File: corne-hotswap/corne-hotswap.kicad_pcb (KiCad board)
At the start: 2 copper layers, 133.8 x 91.7 mm, 49 parts, among them J1 Battery Connector, J2 nice!view, J3 USB_C_Receptacle_PowerOnly_6P, J4 Battery Wire, SW1 SW_Push, SW10 SW_Push, SW11 SW_Push, SW12 SW_Push, SW13 SW_Push, SW14 SW_Push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

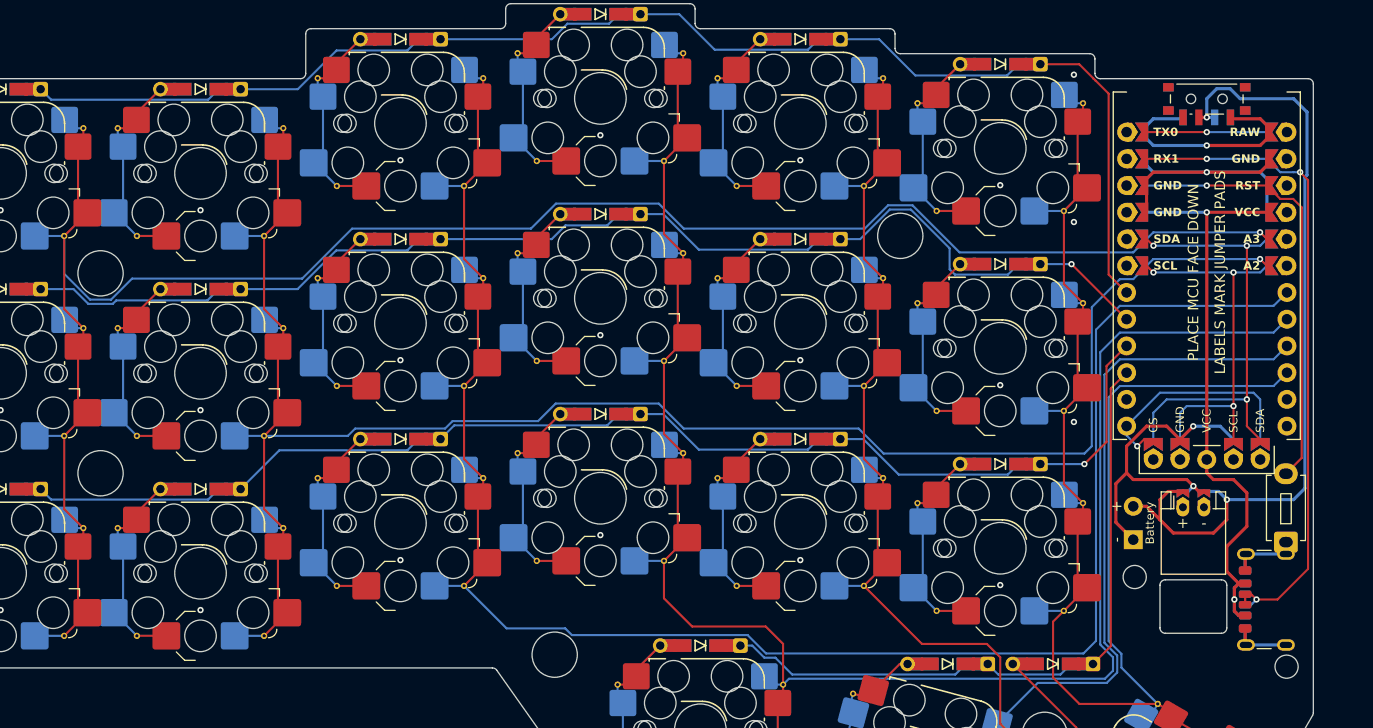
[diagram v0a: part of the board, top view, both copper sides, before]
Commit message: new design (using module)
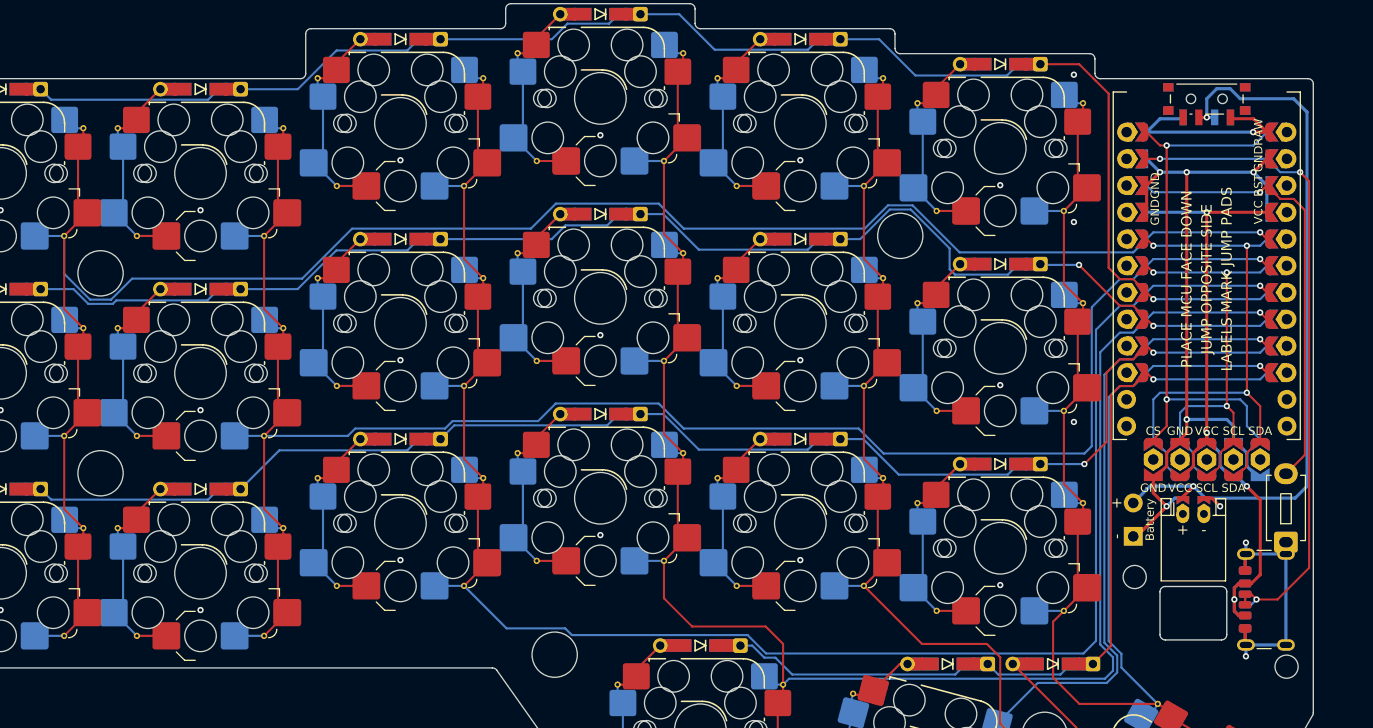
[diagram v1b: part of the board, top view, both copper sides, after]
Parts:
- moved J1 0.63 mm to (162.4, 82.4)
- moved J4 0.32 mm to (157.6, 84.5)
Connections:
- U1 pad 1: unconnected-(U1-D3-TX-Pad1)_1 -> CS
- U1 pad 12: CS -> unconnected-(U1-B5-Pad12)
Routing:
- net CS: track 22.2 -> 52.5 mm, vias 1 -> 2
- net GND: track 78.5 -> 99.6 mm, vias 24 -> 29
- net row1: track 106.2 -> 120.0 mm, vias 1 -> 2
- net row3: track 60.7 -> 74.2 mm, vias 0 -> 1
- net row0: track 120.2 -> 133.7 mm, vias 0 -> 1
- net row2: track 109.1 -> 122.5 mm, vias 1 -> 2
- net unconnected-(U1-D3-TX-Pad1)_1: track 11.4 -> 0.00 mm, vias 1 -> 0
- net SDA: track 42.9 -> 53.6 mm
- net SCL: track 35.7 -> 45.1 mm
- net battery: track 77.1 -> 69.4 mm
- net VCC: track 59.9 -> 64.9 mm, vias 2 -> 4
- net RAW: track 22.1 -> 19.5 mm
- net col5: track 85.8 -> 84.4 mm, vias 0 -> 1
- net col3: track 121.3 -> 119.9 mm, vias 0 -> 1
- net col2: track 131.4 -> 130.0 mm, vias 0 -> 1
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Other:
- outline, holes or cut-outs redrawn

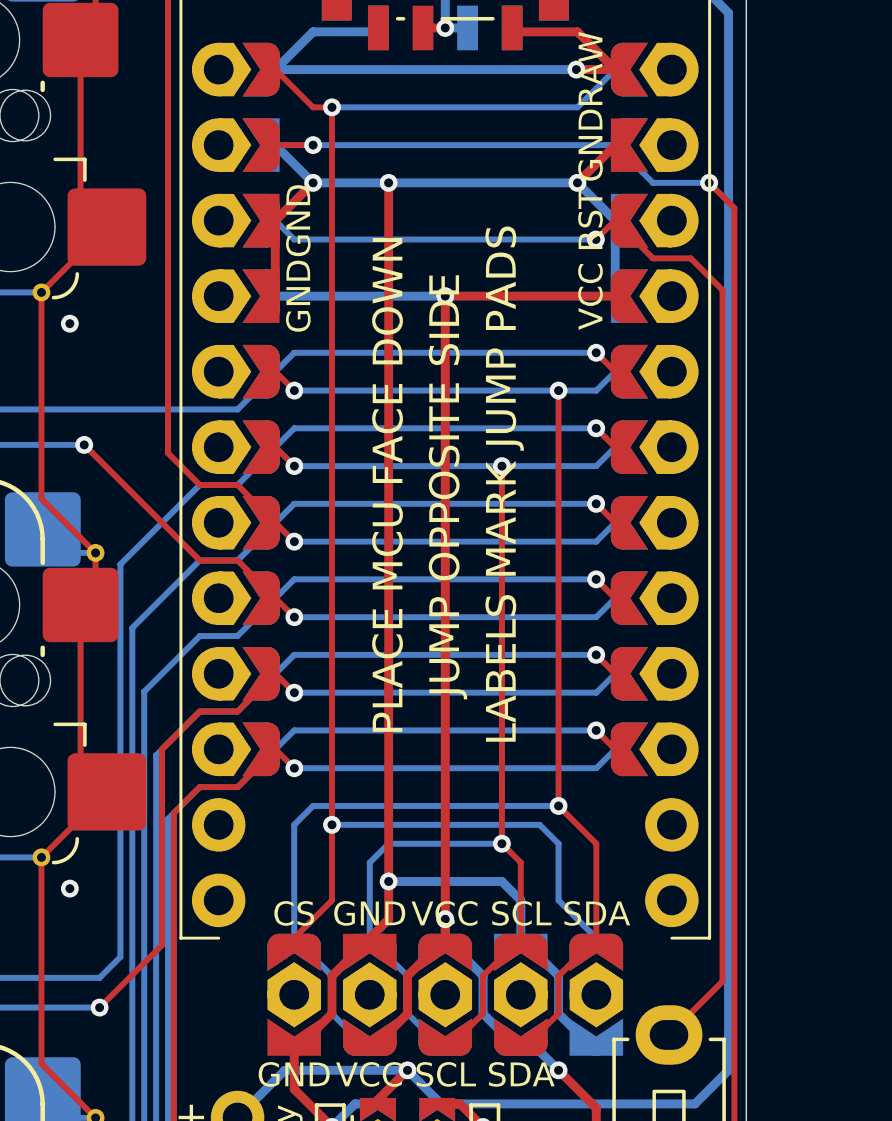
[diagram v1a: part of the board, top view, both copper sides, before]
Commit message: wiring update
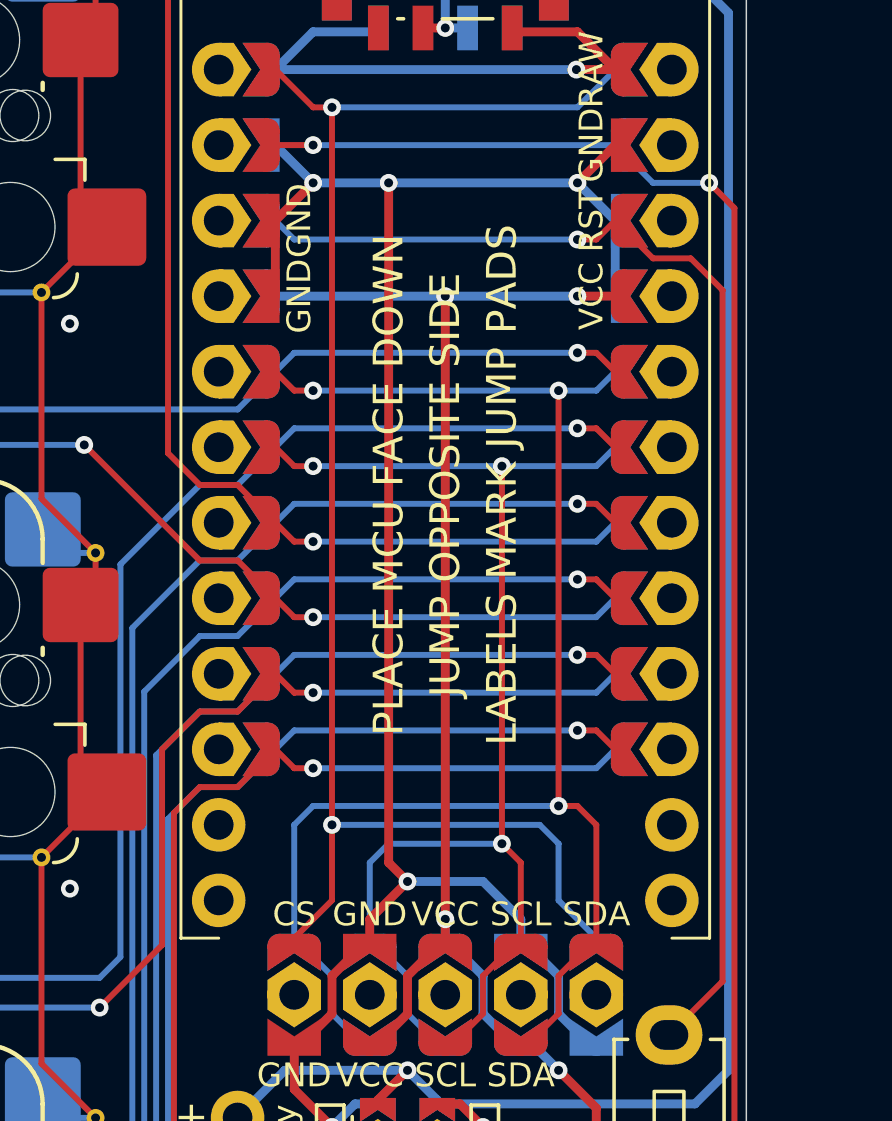
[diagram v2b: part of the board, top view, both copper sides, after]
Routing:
- net VCC: track 64.9 -> 64.8 mm, vias 4 -> 5
